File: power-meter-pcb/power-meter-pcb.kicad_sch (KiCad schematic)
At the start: 25 parts, among them J1 Crank interconnect, J2 Debug, SW1 EN, SW2 BOOT, U1 ESP32-S3-WROOM-1, U2 P3T1755

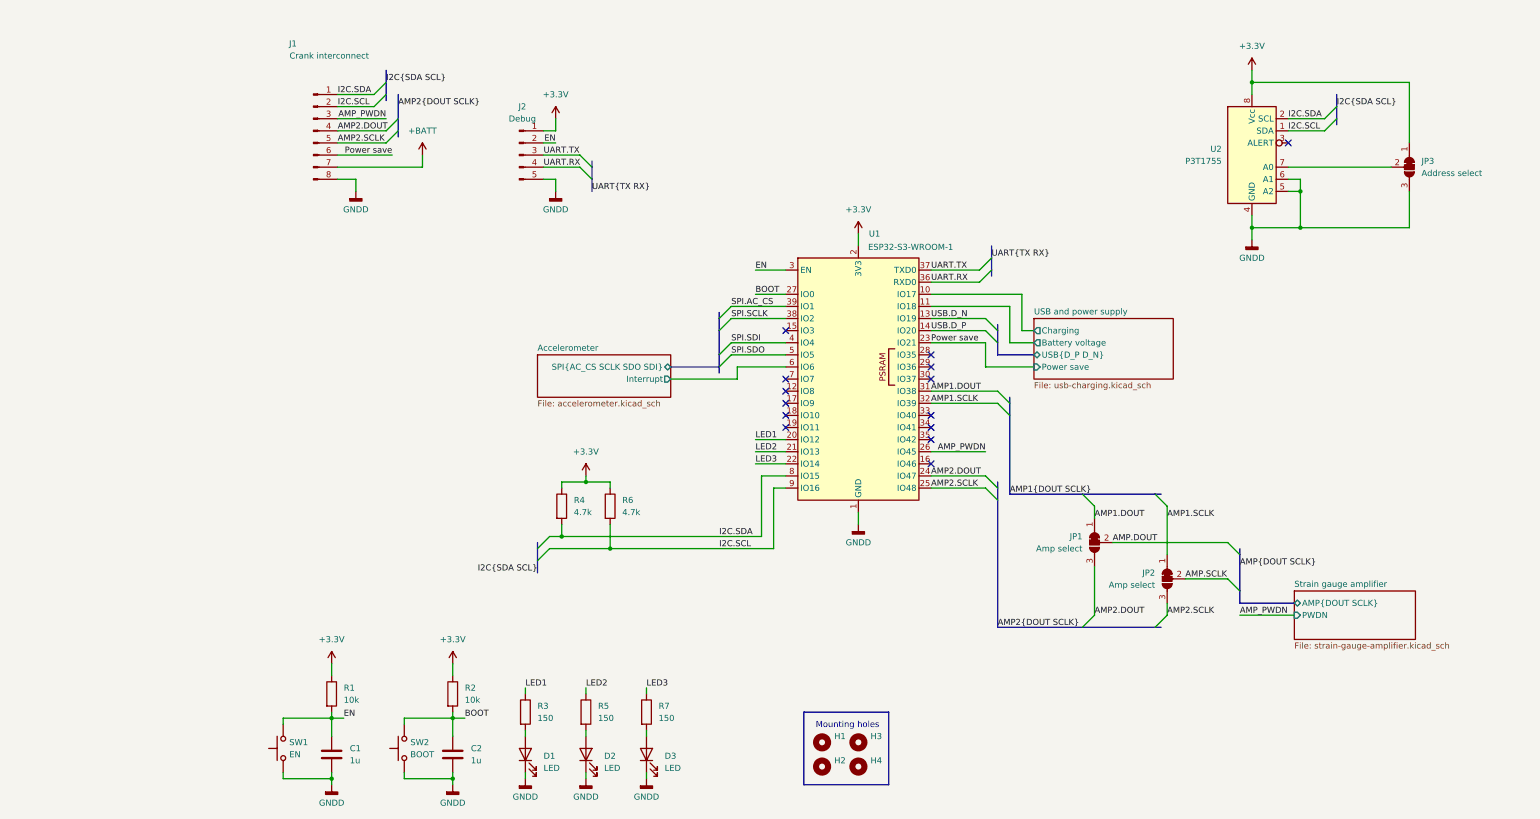
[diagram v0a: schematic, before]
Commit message: Layout almost done, but will likely swap to a 4 layer PCB
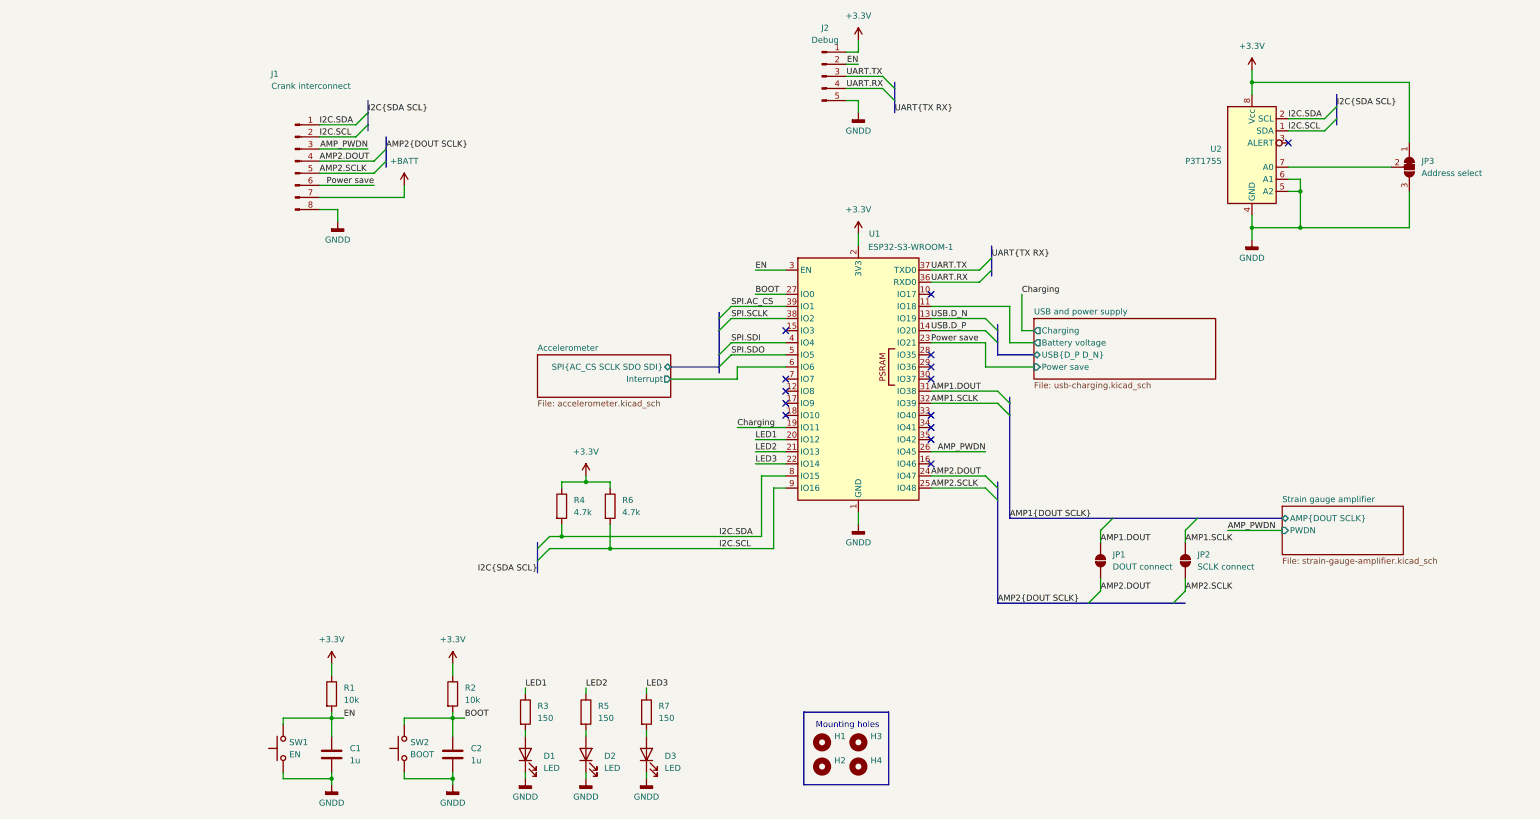
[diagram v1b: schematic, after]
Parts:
- removed JP1, JP2: Amp select, Jumper:SolderJumper-3_P1.3mm_Open_RoundedPad1.0x1.5mm, symbol Jumper:SolderJumper_3_Bridged12
- added JP1: DOUT connect, Jumper:SolderJumper-2_P1.3mm_Open_RoundedPad1.0x1.5mm, symbol Jumper:SolderJumper_2_Open
- added JP2: SCLK connect, Jumper:SolderJumper-2_P1.3mm_Open_RoundedPad1.0x1.5mm, symbol Jumper:SolderJumper_2_Open
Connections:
- net AMP1.DOUT: now also JP1.2 (B)
- net AMP1.SCLK: now also JP2.2 (B)
- net AMP2.DOUT: now also JP1.1 (A)
- net AMP2.SCLK: now also JP2.1 (A)
- net Charging: now reaches U1.19 (IO11)
- net USB and power supply/Charging: no longer names the net of U1.10 (IO17)
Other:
- moved on the sheet: J1, J2

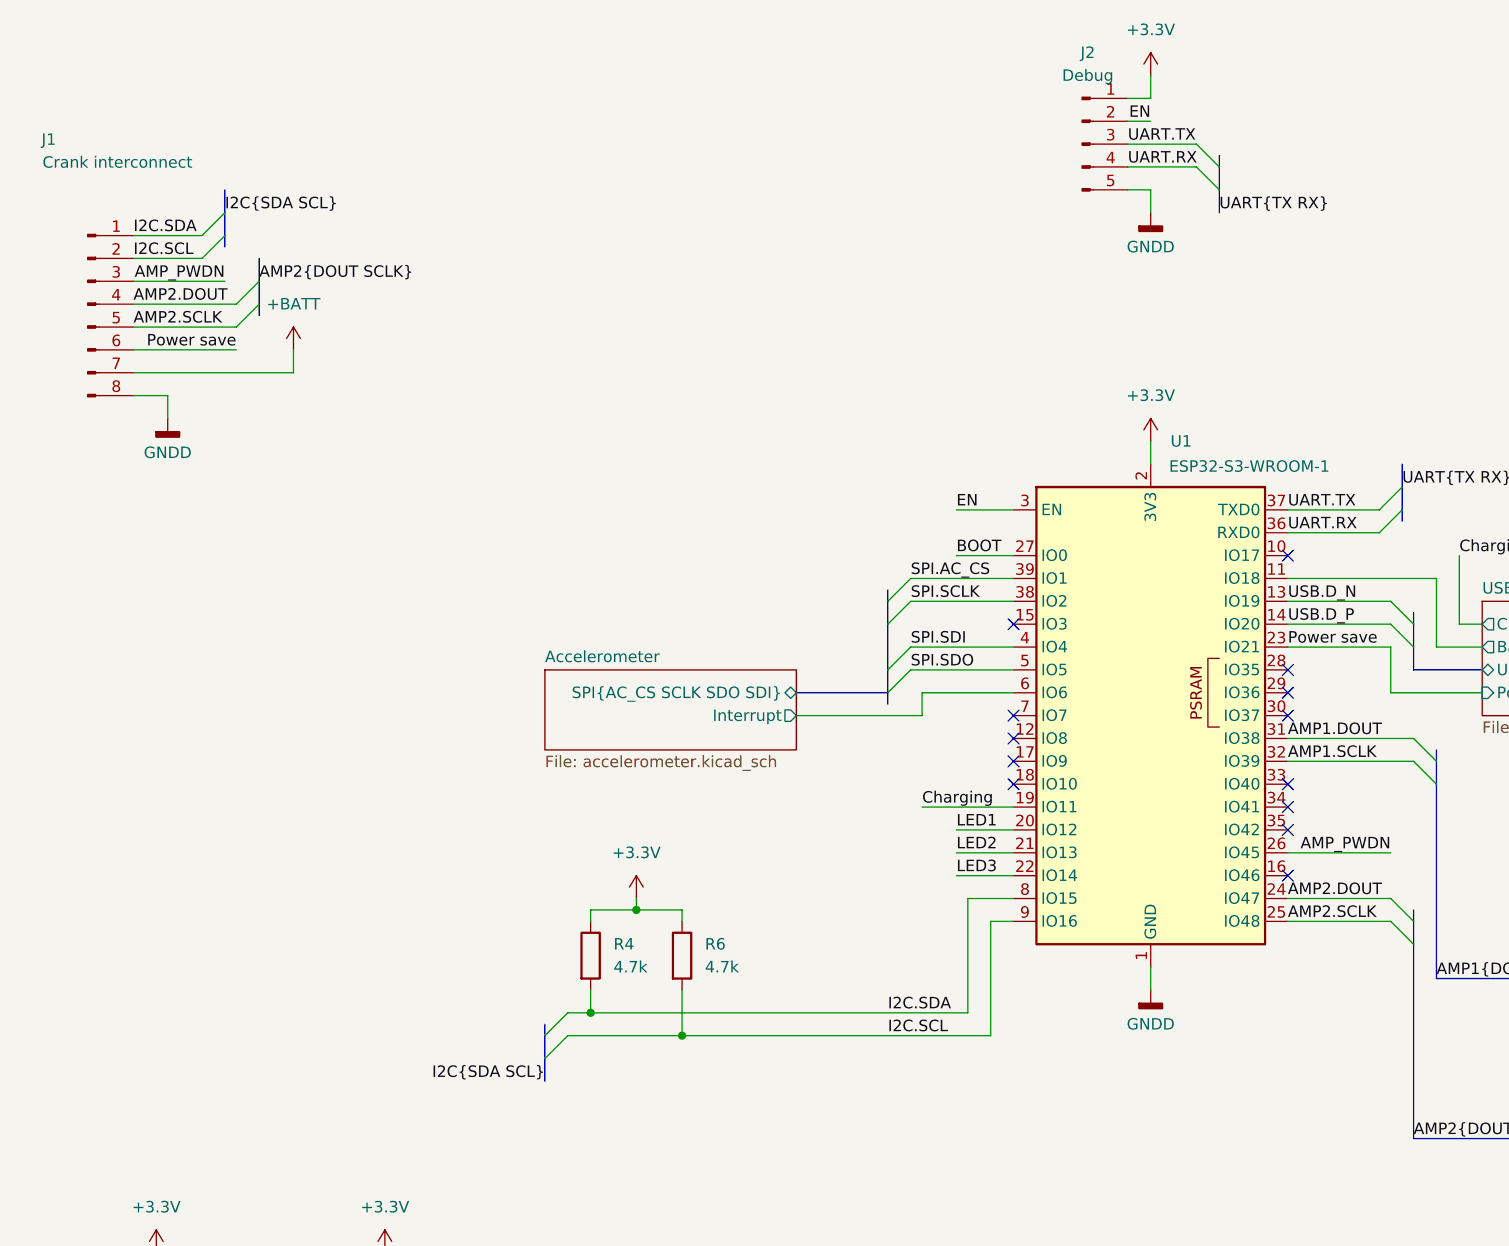
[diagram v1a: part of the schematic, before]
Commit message: Cleaning up PCB back and title box
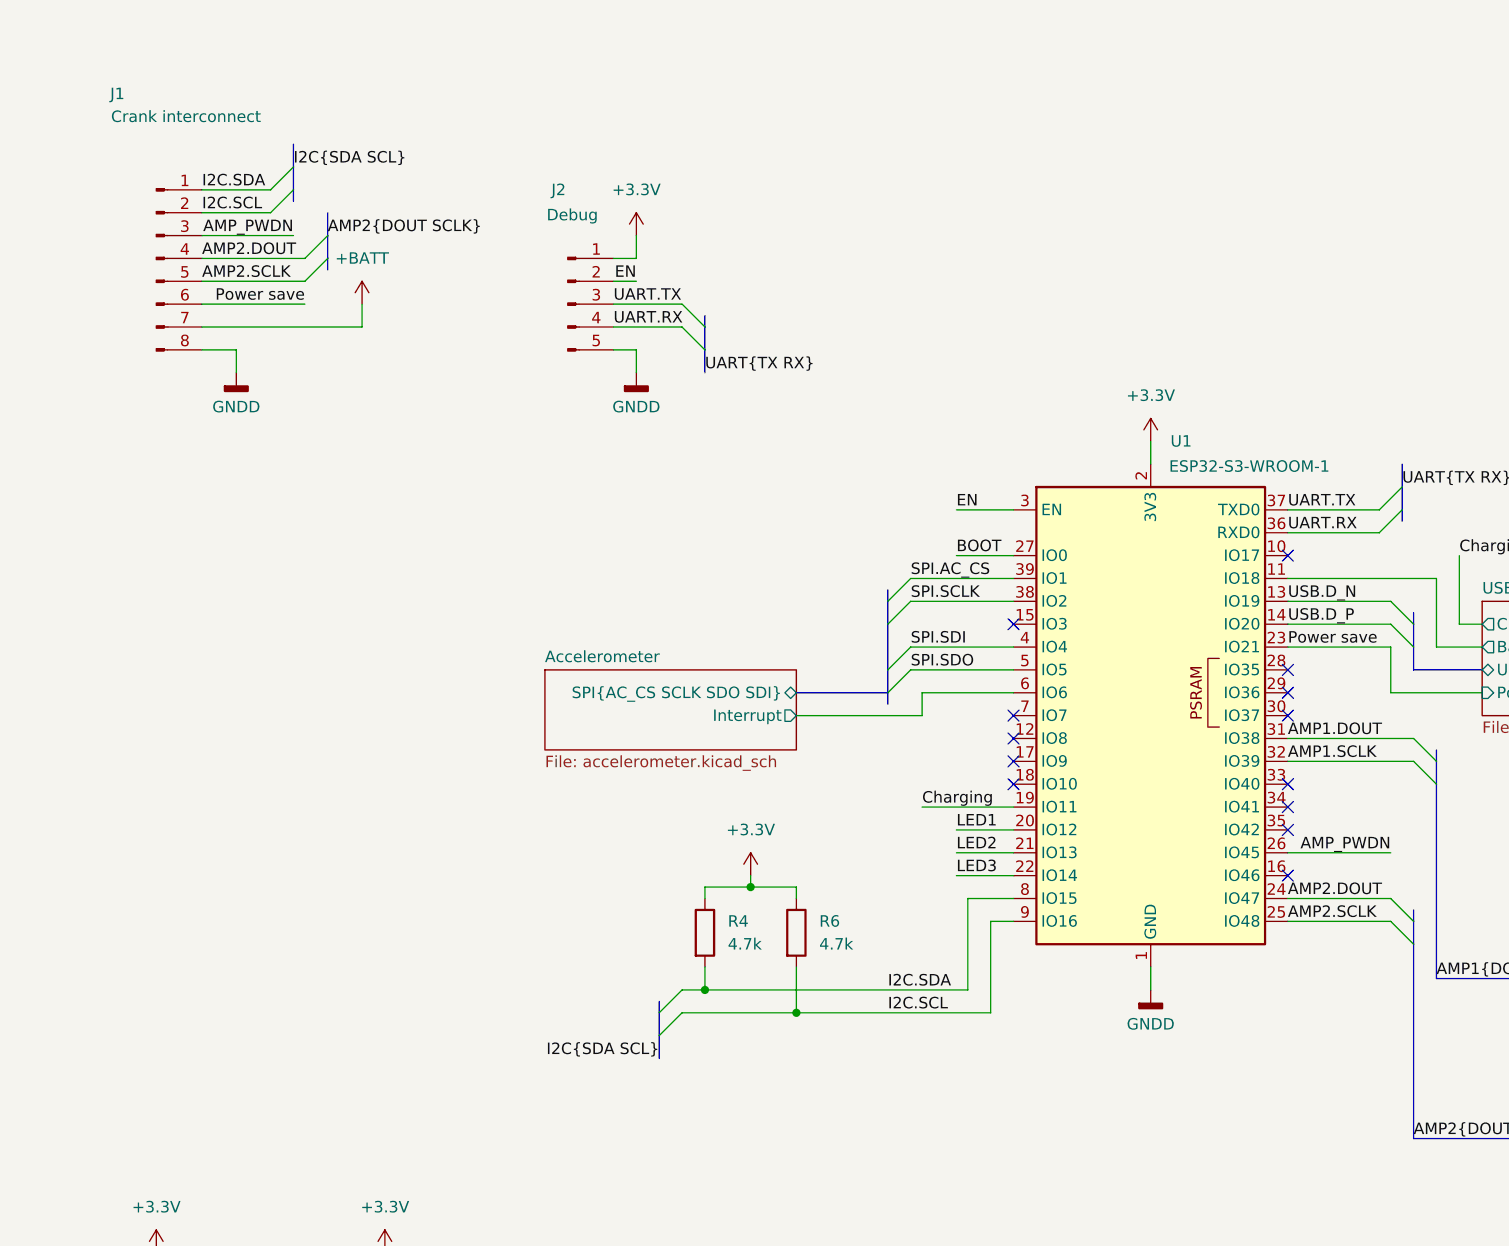
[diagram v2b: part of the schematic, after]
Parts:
- C1, C2, D1, D2, D3, J2, R1, R2, R3, R4, R5, R6, R7, SW1, SW2, U1: PlaceOnSecondary (none) -> No
- H1, H2, H3, H4, J1, JP1, JP2, JP3, U2: PlaceOnSecondary (none) -> Yes
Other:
- moved on the sheet: J1, J2, R4, R6

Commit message: Smaller PCB design started
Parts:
- removed U1: ESP32-S3-WROOM-1, RF_Module:ESP32-S3-WROOM-1, symbol RF_Module:ESP32-S3-WROOM-1
- added U8: ESP32-S3-MINI-1, RF_Module:ESP32-S2-MINI-1, symbol RF_Module:ESP32-S3-MINI-1
- D3, R7: now not fitted; now left out of the parts list
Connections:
- net +3.3V: now also U8.3 (3V3)
- net AMP1.DOUT: now also U8.34 (IO38)
- net AMP1.SCLK: now also U8.35 (IO39)
- net AMP2.DOUT: now also U8.27 (IO47)
- net AMP2.SCLK: now also U8.30 (IO48)
- net AMP_PWDN: now also U8.41 (IO45)
- net Accelerometer/Interrupt: now also U8.10 (IO6)
- net BOOT: now also U8.4 (IO0)
- net EN: now also U8.45 (EN)
- net GNDD: now also U8.1 (GND), U8.2 (GND), U8.42 (GND), U8.43 (GND), U8.46 (GND), U8.47 (GND), U8.48 (GND), U8.49 (GND), U8.50 (GND), U8.51 (GND), U8.52 (GND), U8.53 (GND), U8.54 (GND), U8.55 (GND), U8.56 (GND), U8.57 (GND), U8.58 (GND), U8.59 (GND), U8.60 (GND), U8.61 (GND), U8.62 (GND), U8.63 (GND), U8.64 (GND), U8.65 (GND)
- net I2C.SCL: now also U8.20 (IO16)
- net I2C.SDA: now also U8.19 (IO15)
- net LED1: now also U8.16 (IO12)
- net LED2: now also U8.17 (IO13)
- net LED3: now also U8.18 (IO14)
- net Power save: now also U8.25 (IO21)
- net SPI.AC_CS: now also U8.5 (IO1)
- net SPI.SCLK: now also U8.6 (IO2)
- net SPI.SDI: now also U8.8 (IO4)
- net SPI.SDO: now also U8.9 (IO5)
- net UART.RX: now also U8.40 (RXD0)
- net UART.TX: now also U8.39 (TXD0)
- net USB and power supply/Battery voltage: now also U8.26 (IO26)
- net USB.D_N: now also U8.23 (IO19)
- net USB.D_P: now also U8.24 (IO20)
- no-connect marks 14 -> 15
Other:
- sheet Strain gauge amplifier ports: added Power save; removed none
- sheet USB and power supply ports: added none; removed Charging, Power save

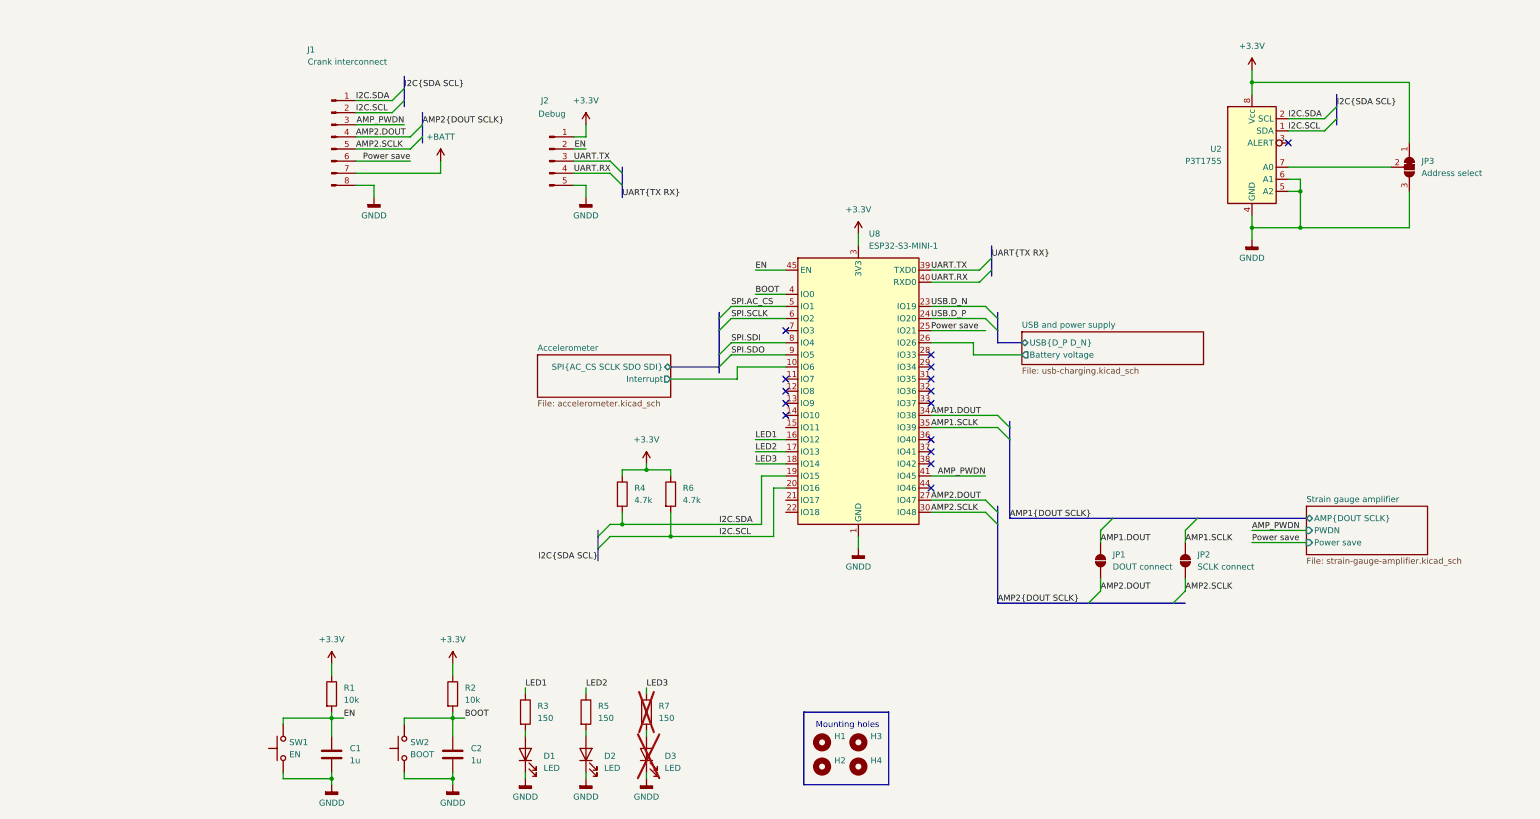
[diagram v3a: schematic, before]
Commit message: Smaller board layout planned
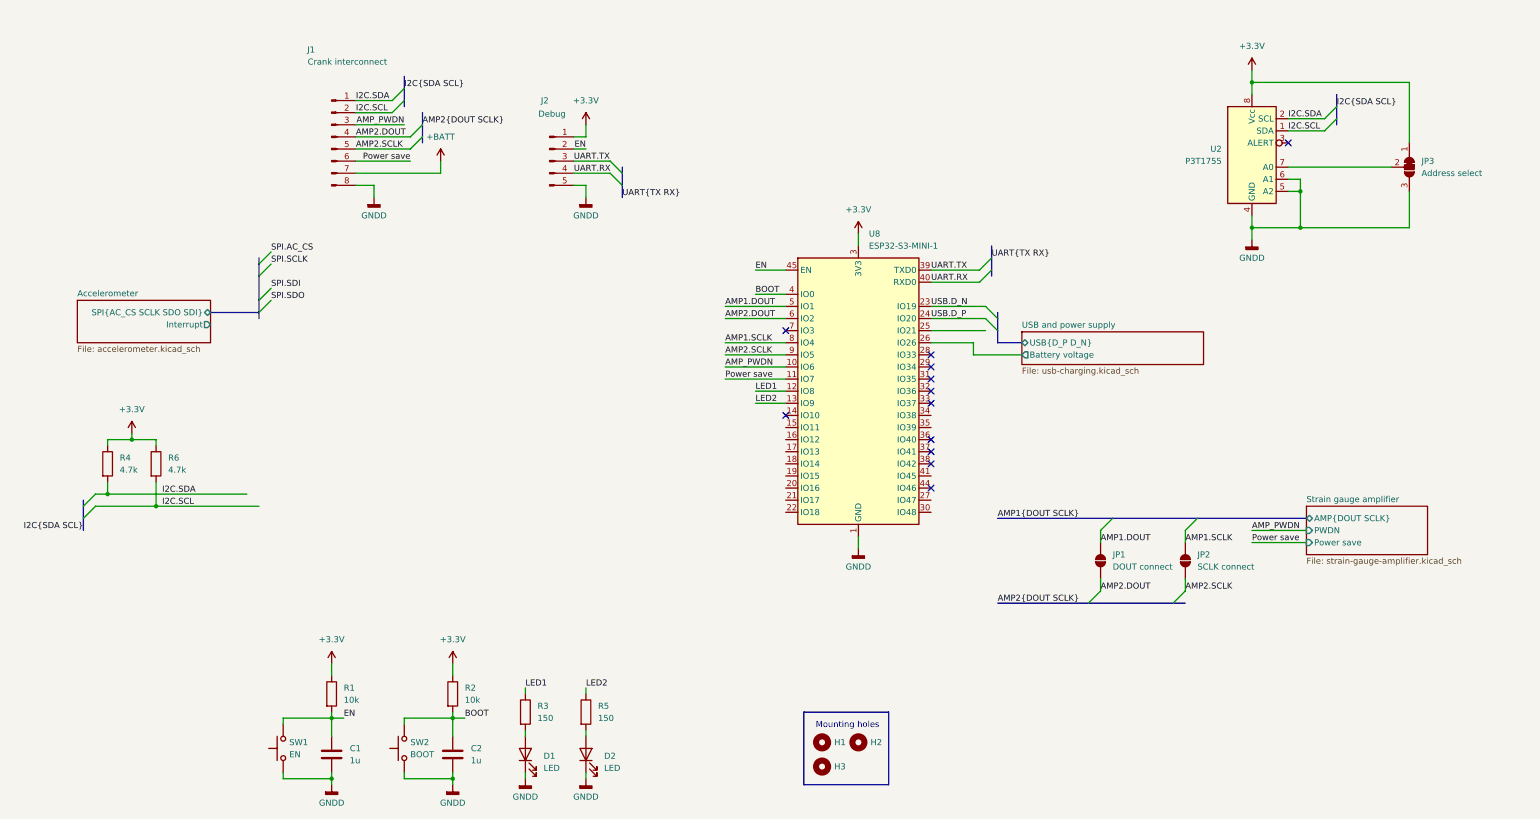
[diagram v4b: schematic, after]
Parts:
- removed D3: LED, LED_SMD:LED_0603_1608Metric_Pad1.05x0.95mm_HandSolder, symbol Device:LED
- removed H1: MountingHole, MountingHole:MountingHole_2.2mm_M2, symbol Mechanical:MountingHole
- removed R7: 150, Resistor_SMD:R_0603_1608Metric_Pad0.98x0.95mm_HandSolder, symbol Device:R
- renumbered H2 to H1, H3 to H2, H4 to H3
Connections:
- net AMP1.DOUT: now also U8.5 (IO1); no longer U8.34 (IO38)
- net AMP1.SCLK: now also U8.8 (IO4); no longer U8.35 (IO39)
- net AMP2.DOUT: now also U8.6 (IO2); no longer U8.27 (IO47)
- net AMP2.SCLK: now also U8.9 (IO5); no longer U8.30 (IO48)
- net AMP_PWDN: now also U8.10 (IO6); no longer U8.41 (IO45)
- net Accelerometer/Interrupt: no longer U8.10 (IO6)
- net I2C.SCL: no longer U8.20 (IO16)
- net I2C.SDA: no longer U8.19 (IO15)
- net LED1: now also U8.12 (IO8); no longer U8.16 (IO12)
- net LED2: now also U8.13 (IO9); no longer U8.17 (IO13)
- net Power save: now also U8.11 (IO7); no longer U8.25 (IO21)
- net SPI.AC_CS: no longer U8.5 (IO1)
- net SPI.SCLK: no longer U8.6 (IO2)
- net SPI.SDI: no longer U8.8 (IO4)
- net SPI.SDO: no longer U8.9 (IO5)
- net LED3: no longer names the net of U8.18 (IO14)
- no-connect marks 15 -> 12
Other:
- moved on the sheet: H1, H3, R4, R6
